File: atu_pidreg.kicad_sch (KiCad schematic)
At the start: 7 parts, among them U21 74HC688, U22 74HC573, U23 74HC541, U6 74HC32, U7 74HC14

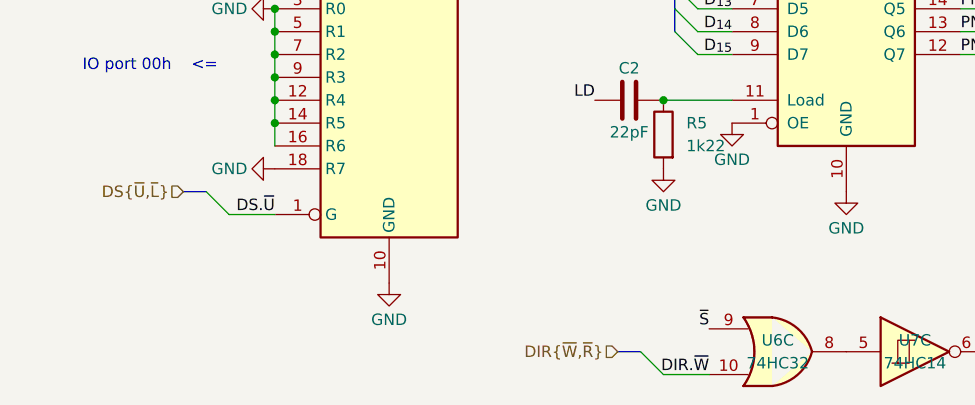
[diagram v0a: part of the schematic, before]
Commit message: finished scheme, footprints not completely assigned yet
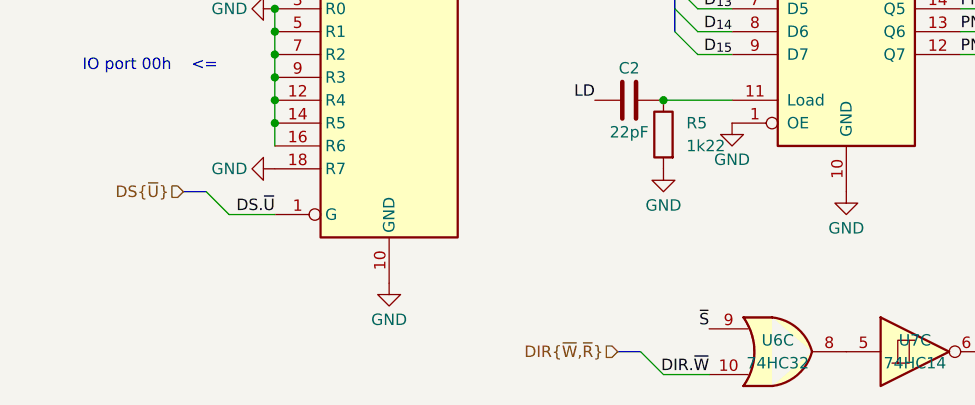
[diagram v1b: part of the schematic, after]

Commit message: done the pcb layout + added the 1M ram bank project
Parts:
- C2: footprint Capacitor_THT:C_Disc_P2.54mm -> Capacitor_THT:C_Disc_D3.0mm_W1.6mm_P2.54mm
- U21: footprint (none) -> Package_DIP:DIP-20_W7.62mm
- U22, U23: footprint Package_DIP:DIP-20_W7.62mm_Socket -> Package_DIP:DIP-20_W7.62mm
- U6, U7: footprint Package_DIP:DIP-14_W7.62mm_Socket -> Package_DIP:DIP-14_W7.62mm
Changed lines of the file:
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@@
 			)
 		)
-		(property "Footprint" "Package_DIP:DIP-20_W7.62mm_Socket"
+		(property "Footprint" "Package_DIP:DIP-20_W7.62mm"
 			(at 152.4 88.9 0)
 			(effects
@@
 			)
 		)
-		(property "Footprint" "Capacitor_THT:C_Disc_P2.54mm"
+		(property "Footprint" "Capacitor_THT:C_Disc_D3.0mm_W1.6mm_P2.54mm"
 			(at 132.08 98.0948 0)
 			(effects
@@
 			)
 		)
-		(property "Footprint" "Package_DIP:DIP-14_W7.62mm_Socket"
+		(property "Footprint" "Package_DIP:DIP-14_W7.62mm"
 			(at 160.02 127 0)
 			(effects
@@
 			)
 		)
-		(property "Footprint" ""
+		(property "Footprint" "Package_DIP:DIP-20_W7.62mm"
 			(at 101.6 88.9 0)
 			(effects
@@
 			)
 		)
-		(property "Footprint" "Package_DIP:DIP-14_W7.62mm_Socket"
+		(property "Footprint" "Package_DIP:DIP-14_W7.62mm"
 			(at 144.78 127 0)
 			(effects
@@
 			)
 		)
-		(property "Footprint" "Package_DIP:DIP-20_W7.62mm_Socket"
+		(property "Footprint" "Package_DIP:DIP-20_W7.62mm"
 			(at 215.9 88.9 0)
 			(effects

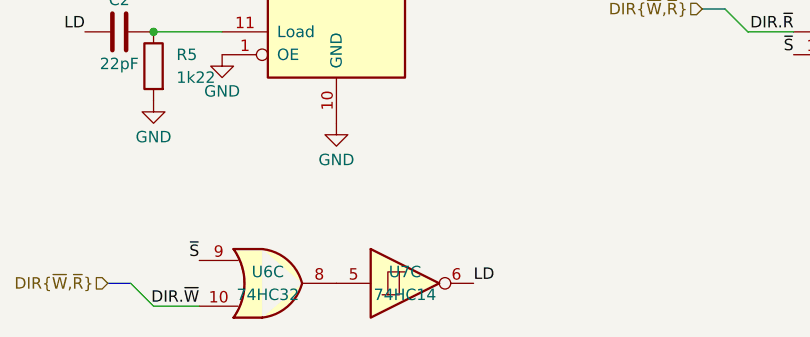
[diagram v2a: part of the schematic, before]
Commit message: updated scheme: 	- fixed E to P & PRT mapping 	- swapped root's 04 couple with the 14's of pidreg & statusreg
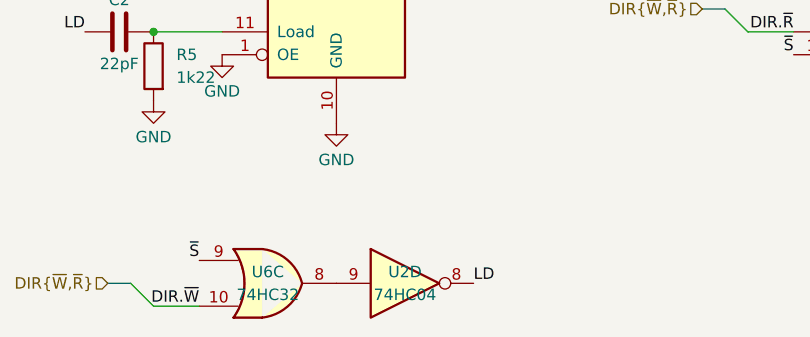
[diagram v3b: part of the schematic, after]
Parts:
- removed U7: 74HC14, Package_DIP:DIP-14_W7.62mm, symbol 74xx:74HC14
- added U2: 74HC04, Package_DIP:DIP-14_W7.62mm, symbol 74xx:74LS04
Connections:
- net LD: now also U2.8
- net at U6.8: now also U2.9
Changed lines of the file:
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@@
-	)
-	(symbol
-		(lib_id "74xx:74HC14")
-		(at 160.02 127 0)
-		(unit 3)
-		(exclude_from_sim no)
-		(in_bom yes)
-		(on_board yes)
-		(dnp no)
-		(property "Reference" "U7"
-			(at 160.02 125.73 0)
-			(effects
-				(font
-					(size 1.27 1.27)
-				)
-			)
-		)
-		(property "Value" "74HC14"
-			(at 160.02 128.27 0)
-			(effects
-				(font
-					(size 1.27 1.27)
-				)
-			)
-		)
-		(property "Footprint" "Package_DIP:DIP-14_W7.62mm"
-			(at 160.02 127 0)
-			(effects
-				(font
-					(size 1.27 1.27)
-				)
-				(hide yes)
-			)
-		)
-		(property "Datasheet" "http://www.ti.com/lit/gpn/sn74HC14"
-			(at 160.02 127 0)
-			(effects
-				(font
-					(size 1.27 1.27)
-				)
-				(hide yes)
-			)
-		)
-		(property "Description" "Hex inverter schmitt trigger"
-			(at 160.02 127 0)
-			(effects
-				(font
-					(size 1.27 1.27)
-				)
-				(hide yes)
-			)
-		)
-		(pin "1"
-		)
-		(pin "5"
-		)
-		(pin "6"
-		)
-		(pin "4"
-		)
-		(pin "2"
-		)
-		(pin "8"
-		)
-		(pin "9"
-		)
-		(pin "3"
-		)
-		(pin "12"
-		)
-		(pin "10"
-		)
-		(pin "7"
-		)
-		(pin "13"
-		)
-		(pin "14"
-		)
-		(pin "11"
-		)
-		(instances
-			(project "SCRM6816"
-				(path "/56448118-82b3-4e1c-bda3-84d63e01a14a/c5c5c8e4-8884-4f58-9370-e357b3396fe5/1aa81d50-fa3e-4844-b0ea-91b73c69a98f"
-					(reference "U7")
-					(unit 3)
-				)
-			)
-		)
 	)
 	(symbol
@@
 				)
 			)
+		)
+	)
+	(symbol
+		(lib_id "74xx:74LS04")
+		(at 160.02 127 0)
+		(unit 4)
+		(exclude_from_sim no)
+		(in_bom yes)
+		(on_board yes)
+		(dnp no)
+		(property "Reference" "U2"
+			(at 160.02 125.73 0)
+			(effects
+				(font
+					(size 1.27 1.27)
+				)
+			)
+		)
+		(property "Value" "74HC04"
+			(at 160.02 128.27 0)
+			(effects
+				(font
+					(size 1.27 1.27)
+				)
+			)
+		)
+		(property "Footprint" "Package_DIP:DIP-14_W7.62mm"
+			(at 160.02 127 0)
+			(effects
+				(font
+					(size 1.27 1.27)
+				)
+				(hide yes)
+			)
+		)
+		(property "Datasheet" "http://www.ti.com/lit/gpn/sn74LS04"
+			(at 160.02 127 0)
+			(effects
+				(font
+					(size 1.27 1.27)
+				)
+				(hide yes)
+			)
+		)
+		(property "Description" "Hex Inverter"
+			(at 160.02 127 0)
+			(effects
+				(font
+					(size 1.27 1.27)
+				)
+				(hide yes)
+			)
+		)
+		(pin "11"
+		)
+		(pin "7"
+		)
+		(pin "5"
+		)
+		(pin "4"
+		)
+		(pin "3"
+		)
+		(pin "2"
+		)
+		(pin "9"
+		)
+		(pin "14"
+		)
+		(pin "6"
+		)
+		(pin "1"
+		)
+		(pin "8"
+		)
+		(pin "10"
+		)
+		(pin "12"
+		)
+		(pin "13"
+		)
+		(instances
+			(project "SCRM6816"
+				(path "/56448118-82b3-4e1c-bda3-84d63e01a14a/c5c5c8e4-8884-4f58-9370-e357b3396fe5/1aa81d50-fa3e-4844-b0ea-91b73c69a98f"
+					(reference "U2")
+					(unit 4)
+				)
+			)

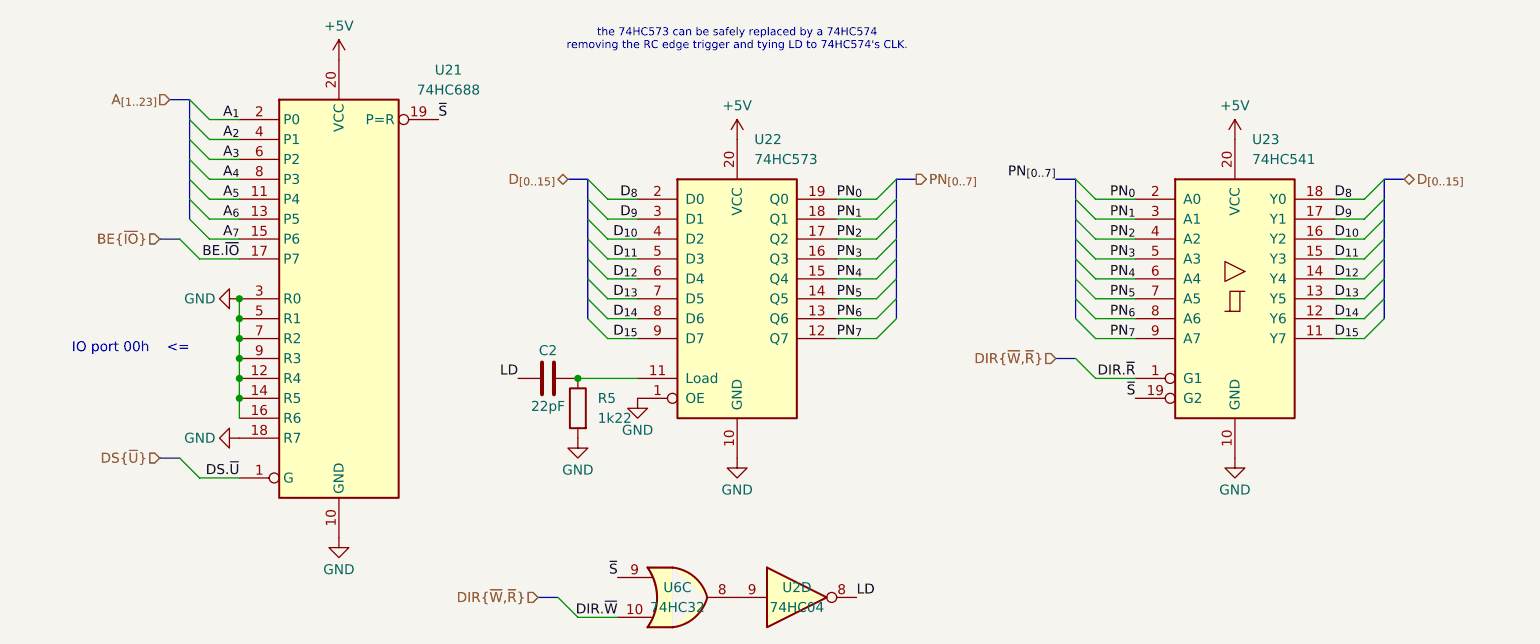
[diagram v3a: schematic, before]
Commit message: first commit: scheme ok [decoder]: 	- new spv. address space [mmu]: 	- removed pidreg 	- switched back to 8Kb mmu rams [ram/peripherals]: 	- added ground pins to connectors [misc]: 	- added DMA support 	- added clock halfer
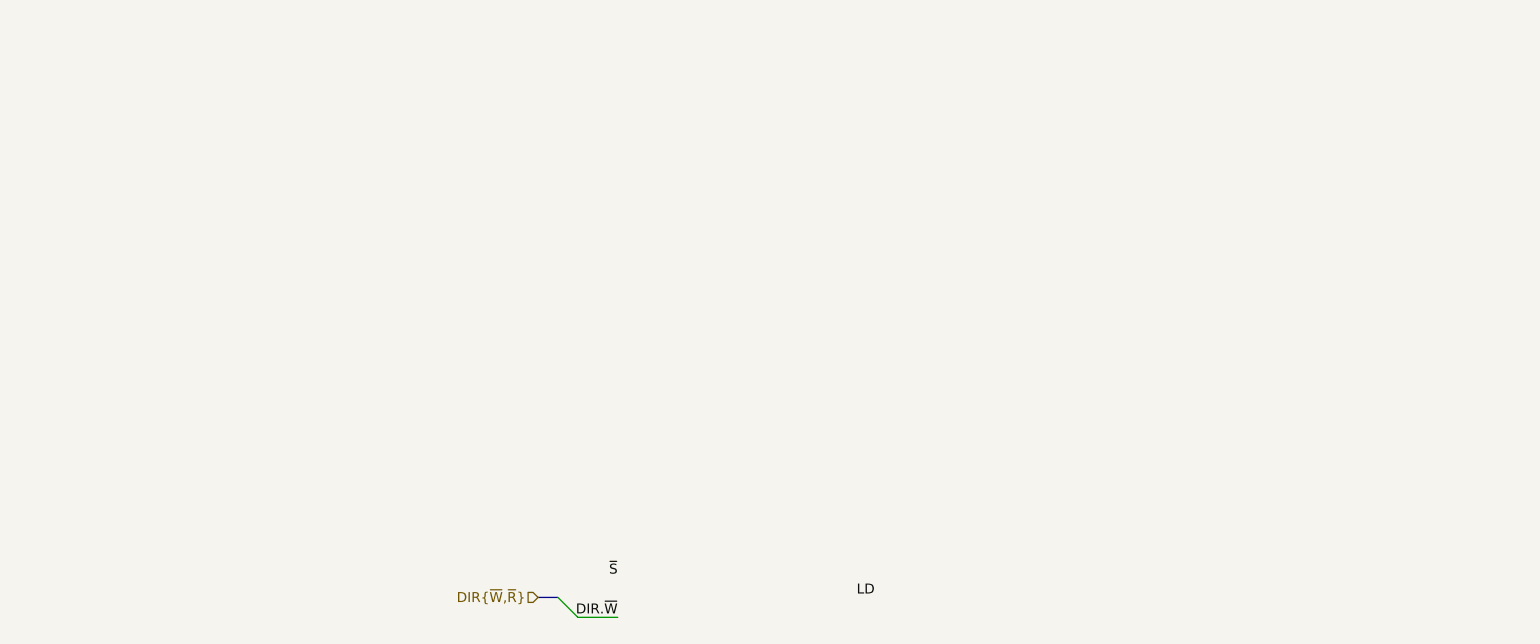
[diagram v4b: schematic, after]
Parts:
- removed C2: 22pF, Capacitor_THT:C_Disc_D3.0mm_W1.6mm_P2.54mm, symbol Device:C
- removed R5: 1k22, Resistor_THT:R_Axial_DIN0207_L6.3mm_D2.5mm_P2.54mm_Vertical, symbol Device:R
- removed U2: 74HC04, Package_DIP:DIP-14_W7.62mm, symbol 74xx:74LS04
- removed U21: 74HC688, Package_DIP:DIP-20_W7.62mm, symbol 74xx:74HC688
- removed U22: 74HC573, Package_DIP:DIP-20_W7.62mm, symbol 74xx:74LS573
- removed U23: 74HC541, Package_DIP:DIP-20_W7.62mm, symbol 74xx:74LS541
- removed U6: 74HC32, Package_DIP:DIP-14_W7.62mm, symbol 74xx:74LS32
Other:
- note removed: "IO port 00h <="
- note removed: "the 74HC573 can be safely replaced by a 74HC574 removing the RC edge trigger and tying LD to 74HC574's CLK."
